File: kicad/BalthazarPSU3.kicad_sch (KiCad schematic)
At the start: 84 parts, among them IC1 BQ24193, J1 AudioIN, J2 USB_C_Receptacle_USB2.0, J3 5-15V / 3-5A, J4 AudioOUT, J7 uC host, J8 5V 3A, J9 12V 2A, Q1 IRF7404, Q2 BSS138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

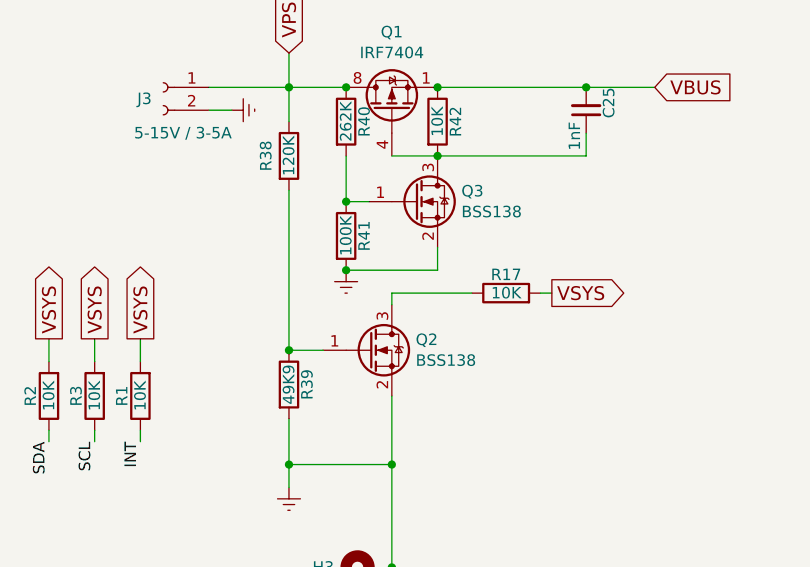
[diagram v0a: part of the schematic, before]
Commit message: Adding production files fix #8
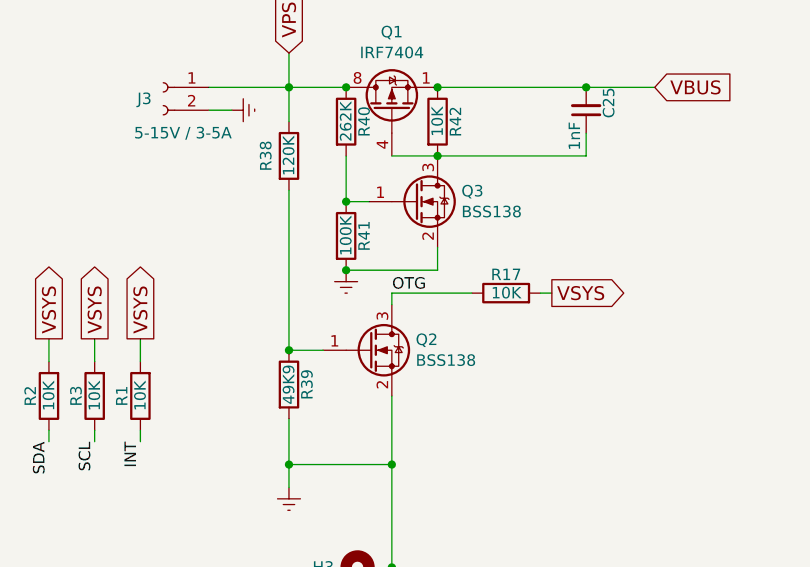
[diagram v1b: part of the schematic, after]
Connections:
- net OTG: now also Q2.3 (D), R17.1
